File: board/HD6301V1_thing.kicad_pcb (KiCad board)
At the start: 2 copper layers, 99.1 x 86.4 mm, 51 parts, among them J1 KMDGX-6S-BS, J2 ps2_i2c, J3 P1_connector, J4 memmap_i2c, J5 8bit_thing_bus_connector, J6 USB_B_Micro, J7 prog_LED, J8 pwr_LED, SW1 Reset, SW2 Banking, U1 APX811-46, U3 SLG46826G, U4 HD6301V1, U5 SLG46826G, U6 74HCT573, U7 IS62C256AL, U8 SST39SF010, U9 74HCS08, X1 CXO_DIP8

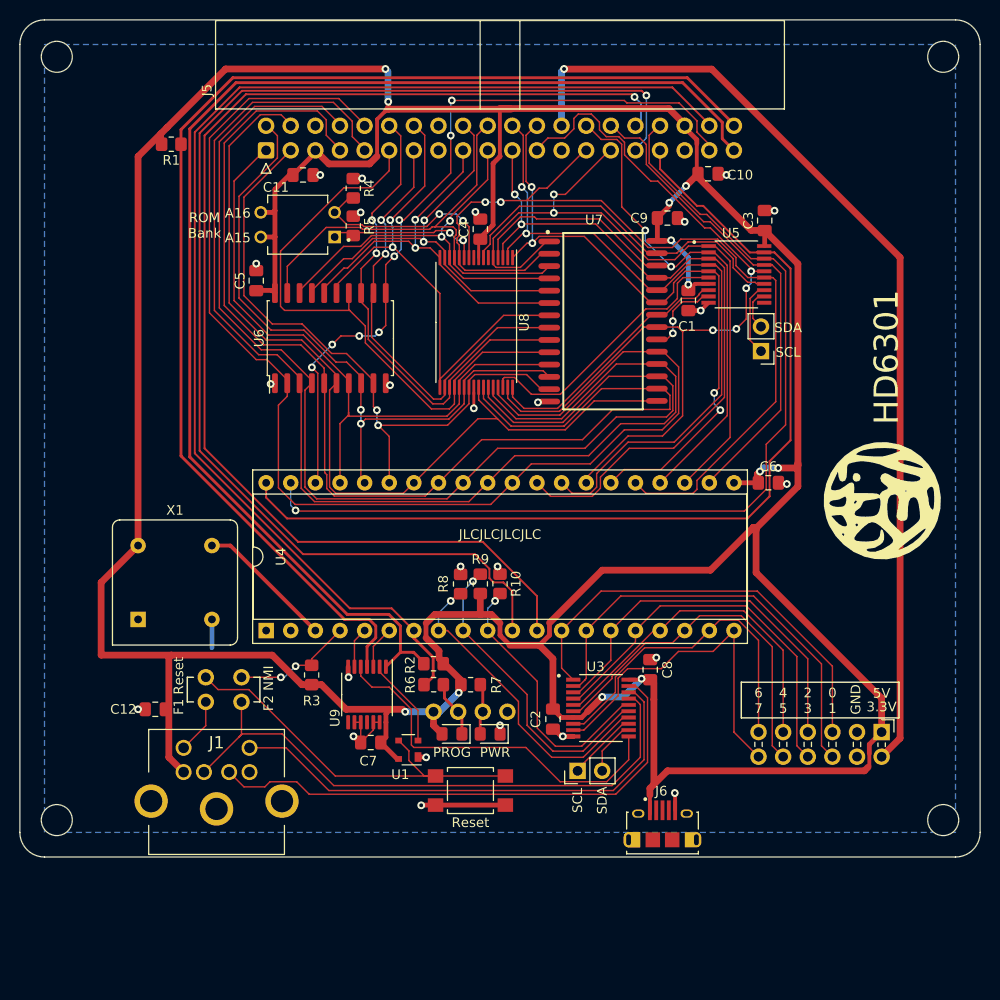
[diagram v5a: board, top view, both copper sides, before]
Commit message: Fix missing pullup on STBYB
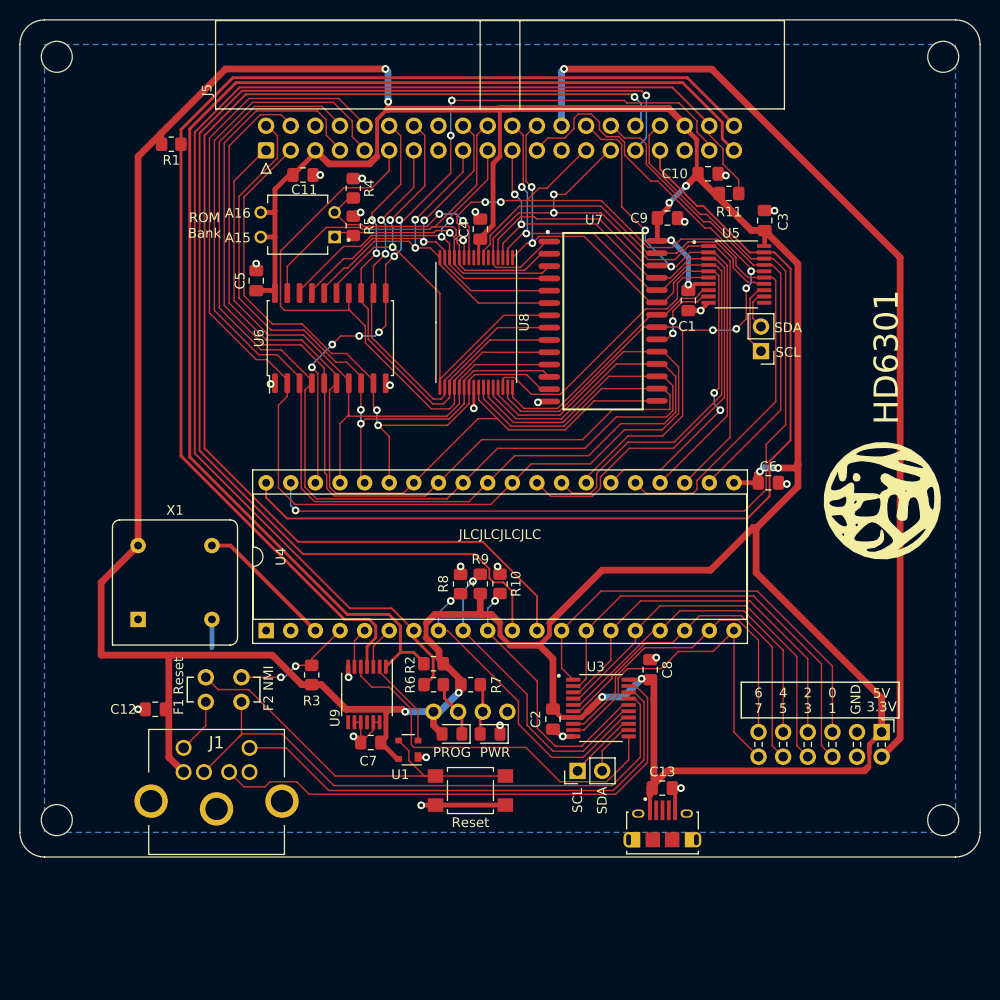
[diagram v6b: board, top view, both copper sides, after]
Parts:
- added C13: 4.7u, Capacitor_SMD:C_0805_2012Metric_Pad1.18x1.45mm_HandSolder, F.Cu at (91.7, 104.6)
- added R11: 10k, Resistor_SMD:R_0805_2012Metric_Pad1.20x1.40mm_HandSolder, F.Cu at (98.6, 43.3)
- R6: value 10k -> 3.3k
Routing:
- net /~{STBY}: track 126.6 -> 134.9 mm
- net GND: track 43.3 -> 44.7 mm
